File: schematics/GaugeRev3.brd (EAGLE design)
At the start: 81 x 81 mm, 36 parts, among them U1 ARDUINO_MINI, U2 VID29, U3 FT232RL-BASICSSOP

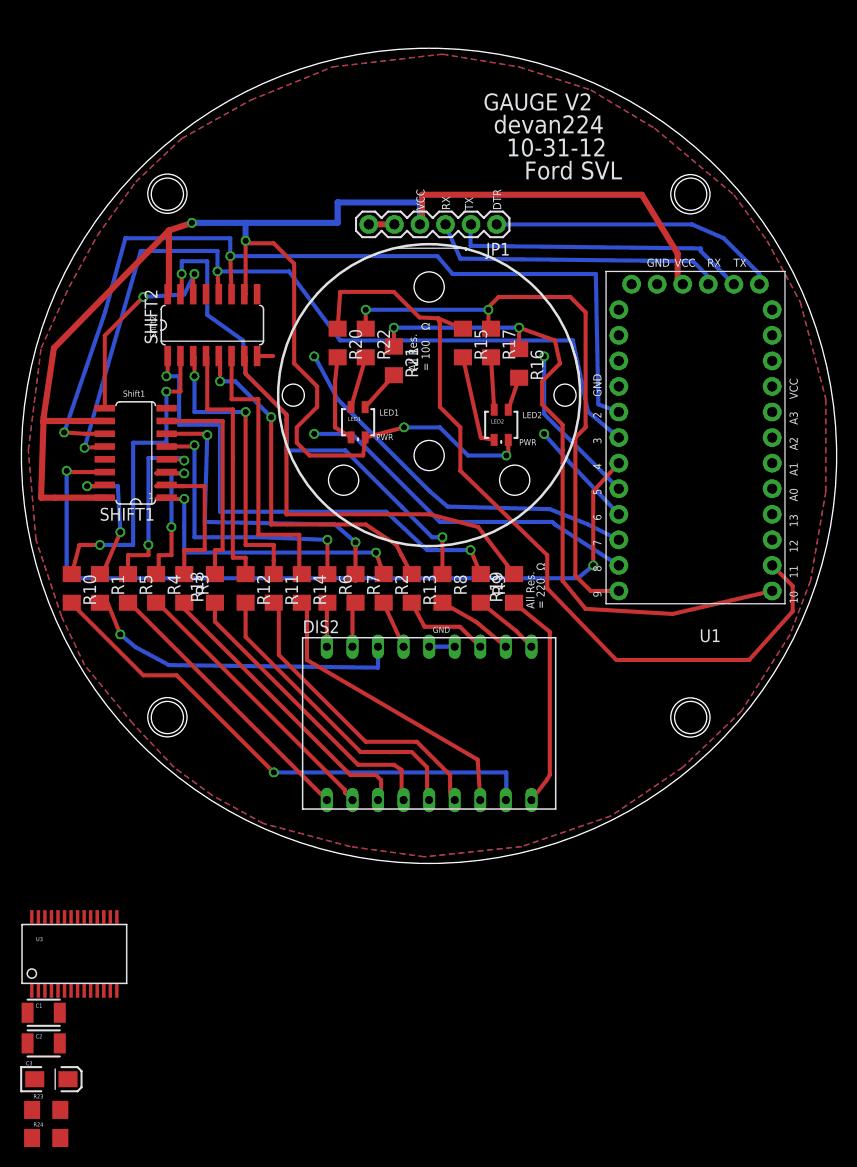
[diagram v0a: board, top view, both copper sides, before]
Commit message: updated schematics
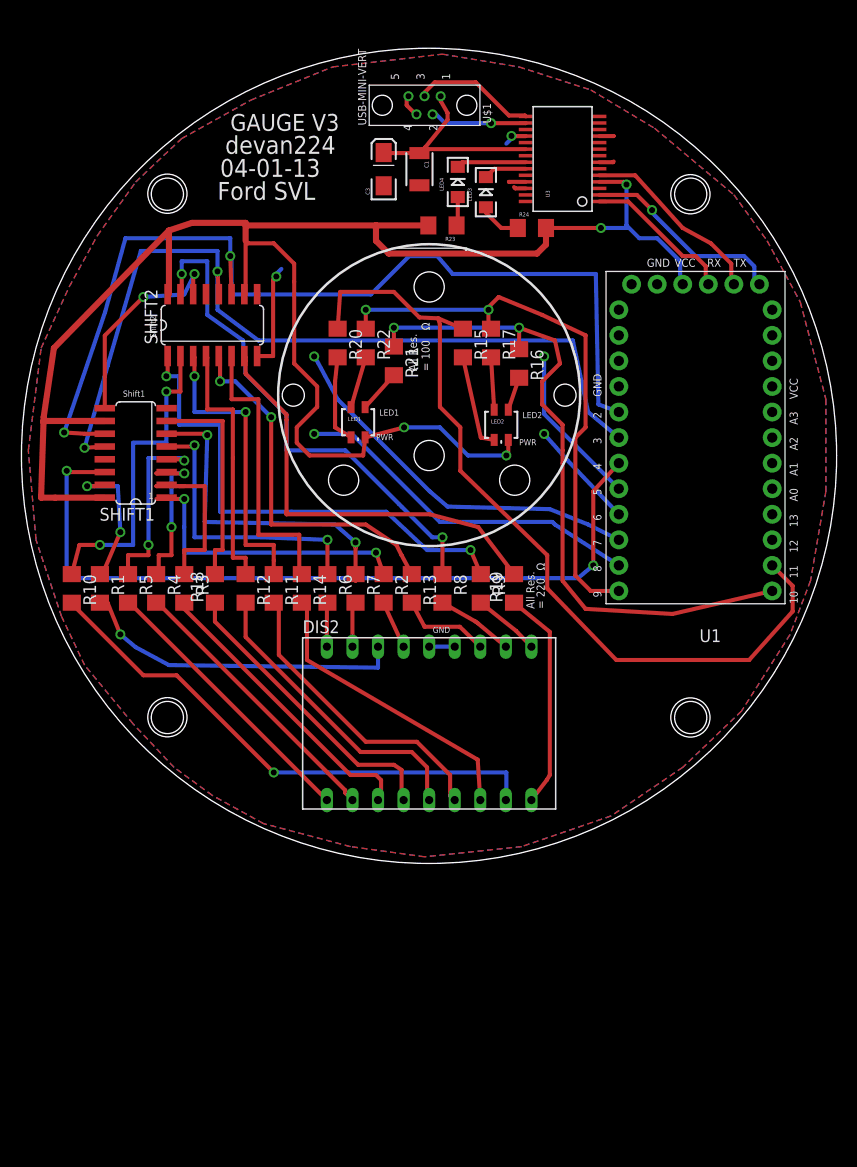
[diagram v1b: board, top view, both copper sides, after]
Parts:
- removed C2: (no value), SparkFun:1210
- removed JP1: (no value), SparkFun:1X06
- added LED3: RED, SparkFun:LED-1206
- added LED4: GRN, SparkFun:LED-1206
- added U$1: USB-MINI-VERT, Evans:USB-MINI-VERT
- C1: value (none) -> .1uF
- C3: value (none) -> 10uF
- moved R24 102.5 mm to (51.3, 64.0)
- moved R23 96.3 mm to (42.4, 64.3), turned to 180 degrees
- moved C3 96.3 mm to (36.6, 69.8), turned to 90 degrees
- moved U3 92.7 mm to (54.4, 70.9), turned to 90 degrees
- moved C1 91.8 mm to (40.1, 69.8), turned to 270 degrees
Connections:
- removed net RX: JP1.3, U1.RX
- removed net TX: JP1.2, U1.TX
- removed net VCCIO: U3.4
- new net D+: U$1.D+, U3.15
- new net D-: U$1.D-, U3.16
- new net N$17: LED3.C, U3.23
- new net N$18: LED4.C, U3.22
- new net N$27: LED4.A, R23.1
- new net N$28: LED3.A, R24.1
- new net RXI: U1.RX, U3.1
- new net TXO: U1.TX, U3.5
- new net VBUS: C1.1, C3.A, U$1.VBUS, U3.20
- net DTR: now also U3.2; no longer JP1.1
- net GND: now also C1.2, C3.C, U$1.GND, U$1.ID, U3.11; no longer JP1.5, JP1.6
- net VCC: now also R23.2, R24.2, U3.4; no longer JP1.4, U3.20
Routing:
- net RX: track 30.0 -> 0.00 mm
- net TX: track 30.0 -> 0.00 mm
- net VBUS: track 0.00 -> 20.5 mm
- net TXO: track 0.00 -> 18.8 mm
- net GND: track 6.67 -> 25.1 mm, vias 0 -> 2
- net RXI: track 0.00 -> 15.1 mm
- net D+: track 0.00 -> 12.3 mm
- net D-: track 0.00 -> 9.63 mm, vias 0 -> 1
- net DTR: track 28.9 -> 20.5 mm, vias 0 -> 1
- net VCC: track 173.1 -> 180.3 mm
- net N$18: track 0.00 -> 6.95 mm
- net CLOCK: track 92.5 -> 97.8 mm
- net N$28: track 0.00 -> 4.34 mm
- net N$17: track 0.00 -> 4.31 mm
- net N$27: track 0.00 -> 2.87 mm
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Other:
- board text added: "04-01-13"
- board text added: "GAUGE V3"
- board text removed: "10-31-12"
- board text removed: "DTR"
- board text removed: "GAUGE V2"
- board text removed: "RX"
- board text removed: "TX"
- board text removed: "VCC"
